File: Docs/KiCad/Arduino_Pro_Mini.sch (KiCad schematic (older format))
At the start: 13 parts, among them P1 Digital, P2 COM, P3 ADC, P4 Analog, P5 ADC, P6 COM, P7 CONN_01X04, P8 CONN_01X03, P9 CONN_01X04, SW1 SW_PUSH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

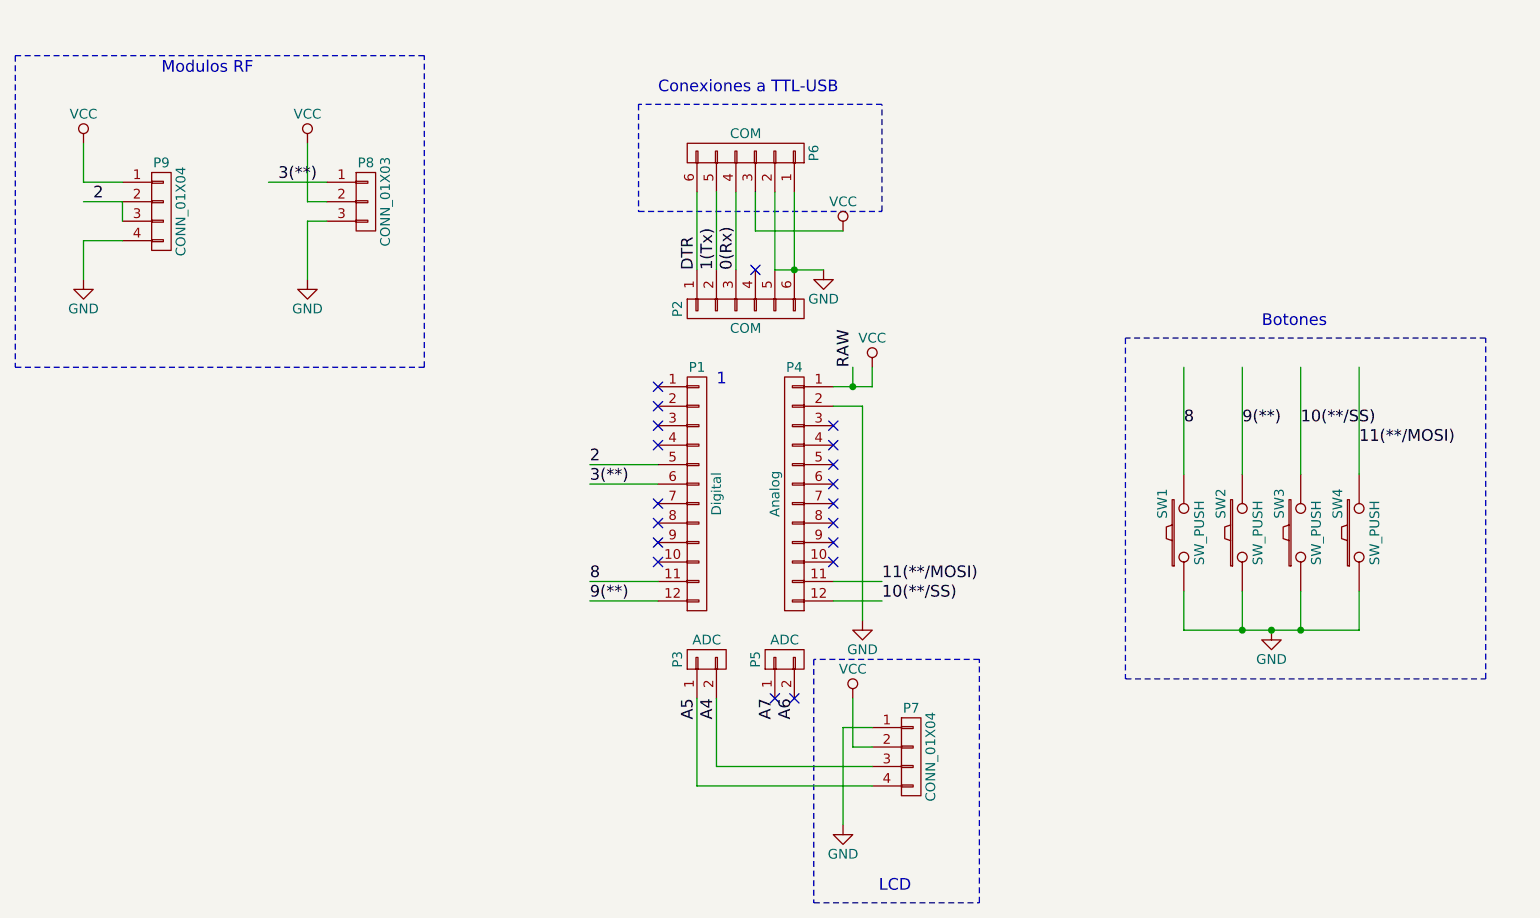
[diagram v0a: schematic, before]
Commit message: Reducida tamaño PCB
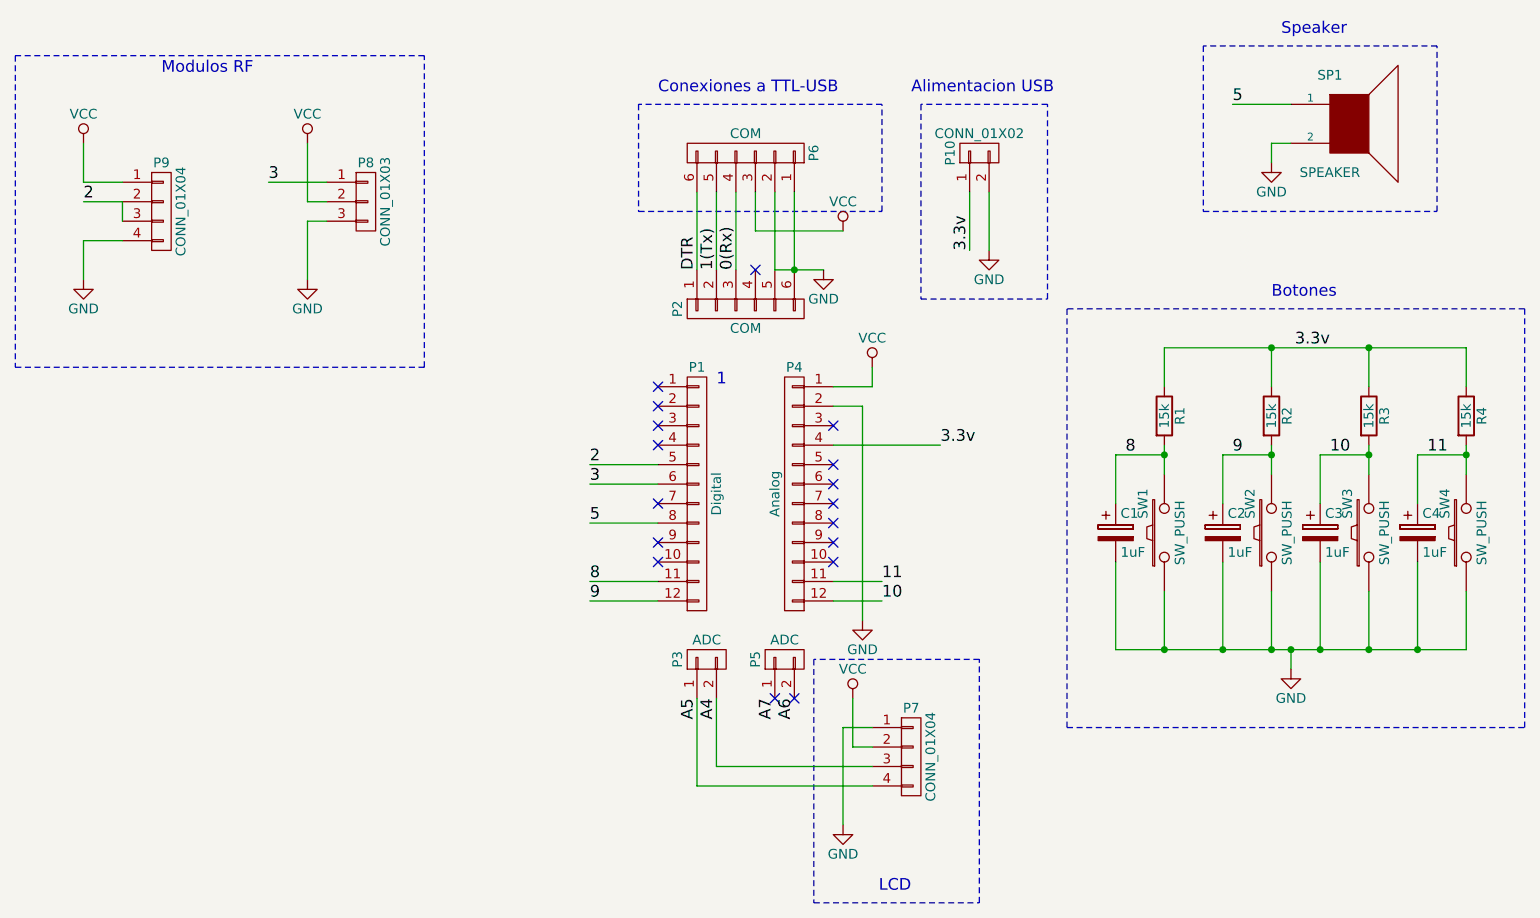
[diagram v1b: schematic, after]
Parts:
- added C1, C2, C3, C4: 1uF, Capacitors_ThroughHole:CP_Radial_D4.0mm_P2.00mm, symbol CP
- added P10: CONN_01X02, Pin_Headers:Pin_Header_Straight_1x02_Pitch2.54mm, symbol CONN_01X02
- added R1, R2, R3, R4: 15k, Resistors_ThroughHole:R_Axial_DIN0207_L6.3mm_D2.5mm_P10.16mm_Horizontal, symbol R
- added SP1: SPEAKER, Buzzers_Beepers:Buzzer_12x9.5RM7.6, symbol SPEAKER
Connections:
- net labels added: 10, 11, 3, 3.3v, 5, 9
- net labels removed: 10(**/SS), 11(**/MOSI), 3(**), 9(**), RAW
- wire segments 47 -> 71
- no-connect marks 19 -> 17
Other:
- note added: "Alimentacion USB"
- note added: "Speaker"
- moved on the sheet: SW1, SW2, SW3, SW4
